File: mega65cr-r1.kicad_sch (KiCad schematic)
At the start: 0 parts

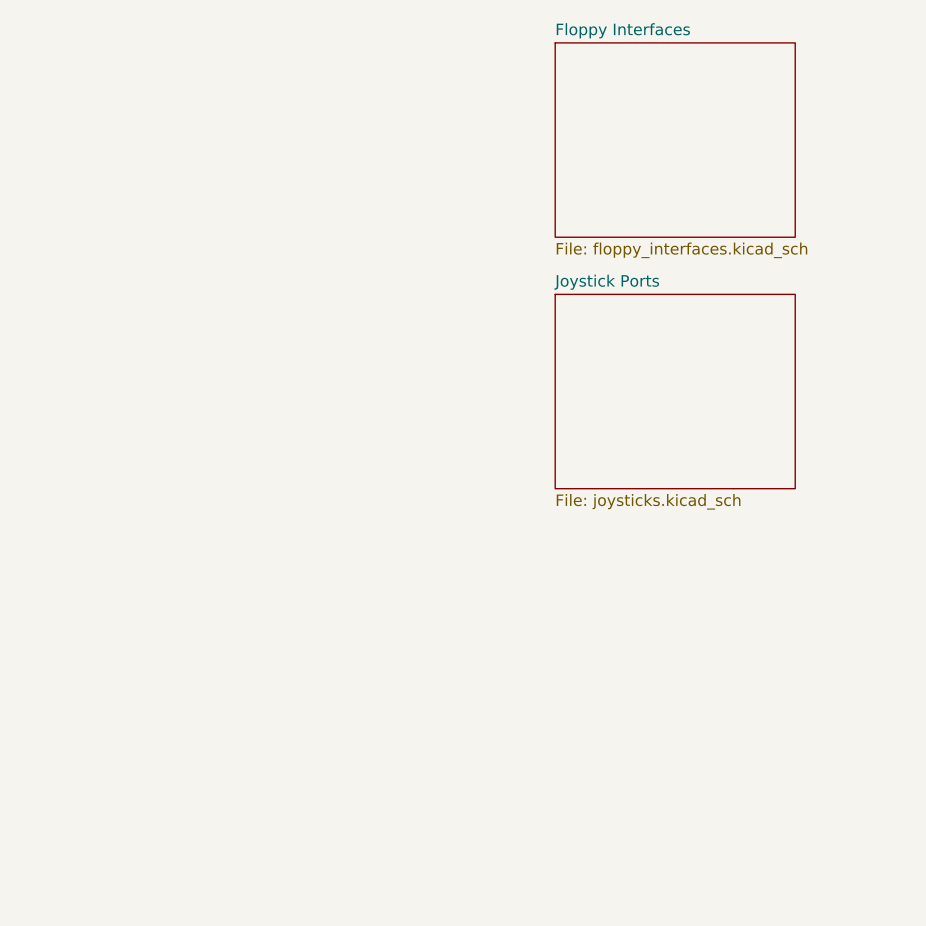
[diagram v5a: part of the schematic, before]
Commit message: add stubs for missing sheets
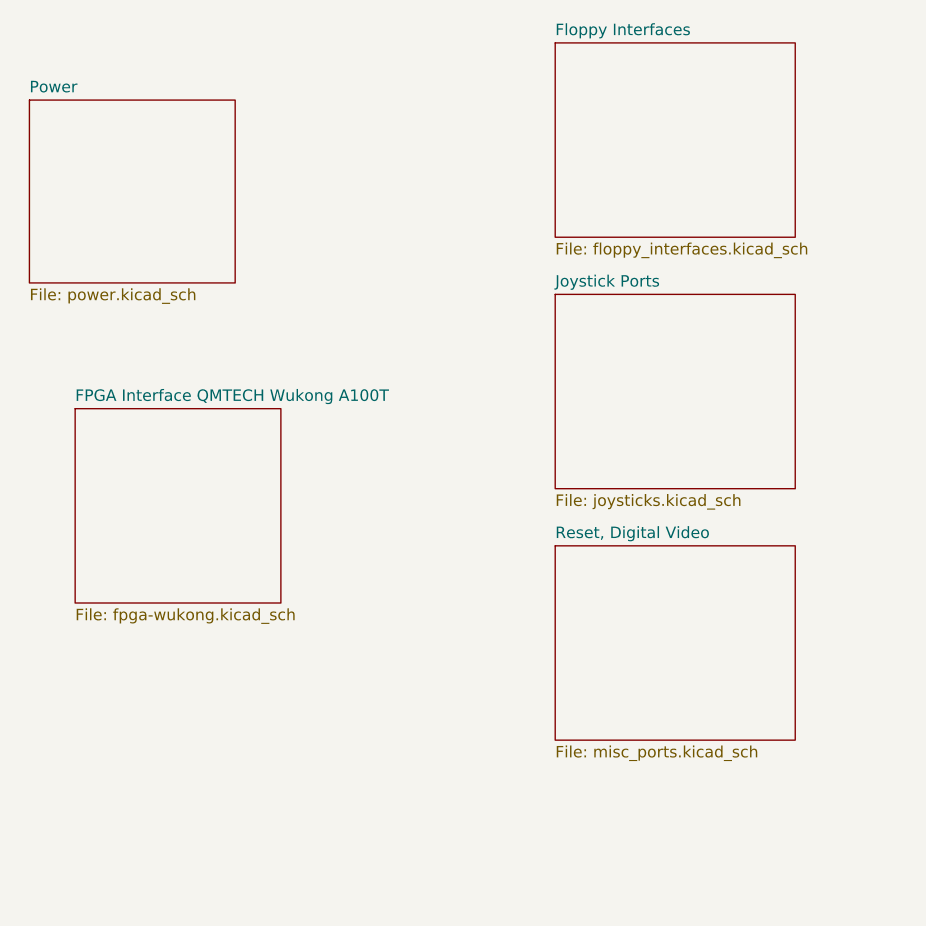
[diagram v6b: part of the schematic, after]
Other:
- added sheet FPGA Interface QMTECH Wukong A100T (fpga-wukong.kicad_sch)
- added sheet Power (power.kicad_sch)
- added sheet Reset, Digital Video (misc_ports.kicad_sch)
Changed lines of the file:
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@@
     (effects (font (size 1.27 1.27)) (justify left bottom))
+  )
+  (sheet (at 195.58 59.69) (size 22.86 21.59) (fields_autoplaced)
+    (stroke (width 0.1524) (type solid) (color 0 0 0 0))
+    (fill (color 0 0 0 0.0000))
+    (property "Sheet name" "FPGA Interface QMTECH Wukong A100T" (id 0) (at 195.58 58.9784 0)
+      (effects (font (size 1.27 1.27)) (justify left bottom))
+    )
+    (property "Sheet file" "fpga-wukong.kicad_sch" (id 1) (at 195.58 81.8646 0)
+      (effects (font (size 1.27 1.27)) (justify left top))
+    )
+  )
+  (sheet (at 248.92 74.93) (size 26.67 21.59) (fields_autoplaced)
+    (stroke (width 0.1524) (type solid) (color 0 0 0 0))
+    (fill (color 0 0 0 0.0000))
+    (property "Sheet name" "Reset, Digital Video" (id 0) (at 248.92 74.2184 0)
+      (effects (font (size 1.27 1.27)) (justify left bottom))
+    )
+    (property "Sheet file" "misc_ports.kicad_sch" (id 1) (at 248.92 97.1046 0)
+      (effects (font (size 1.27 1.27)) (justify left top))
+    )
   )
   (sheet (at 248.92 19.05) (size 26.67 21.59) (fields_autoplaced)
@@
     )
     (property "Sheet file" "floppy_interfaces.kicad_sch" (id 1) (at 248.92 41.2246 0)
+      (effects (font (size 1.27 1.27)) (justify left top))
+    )
+  )
+  (sheet (at 190.5 25.4) (size 22.86 20.32) (fields_autoplaced)
+    (stroke (width 0.1524) (type solid) (color 0 0 0 0))
+    (fill (color 0 0 0 0.0000))
+    (property "Sheet name" "Power" (id 0) (at 190.5 24.6884 0)
+      (effects (font (size 1.27 1.27)) (justify left bottom))
+    )
+    (property "Sheet file" "power.kicad_sch" (id 1) (at 190.5 46.3046 0)
       (effects (font (size 1.27 1.27)) (justify left top))
     )
@@
     (path "/bf6f0944-6234-4b84-bc75-6d48246ce101" (page "2"))
     (path "/ee5f4bc8-ae5c-44e7-a23d-2b06f471a294" (page "3"))
+    (path "/46f1890f-c5bb-4aae-8808-0511f47e29d8" (page "4"))
+    (path "/cd7afc30-e644-4a23-9f17-325d3146c7db" (page "5"))
+    (path "/2879178d-3b15-409b-b355-34424f0e3bd8" (page "6"))
   )
   (symbol_instances

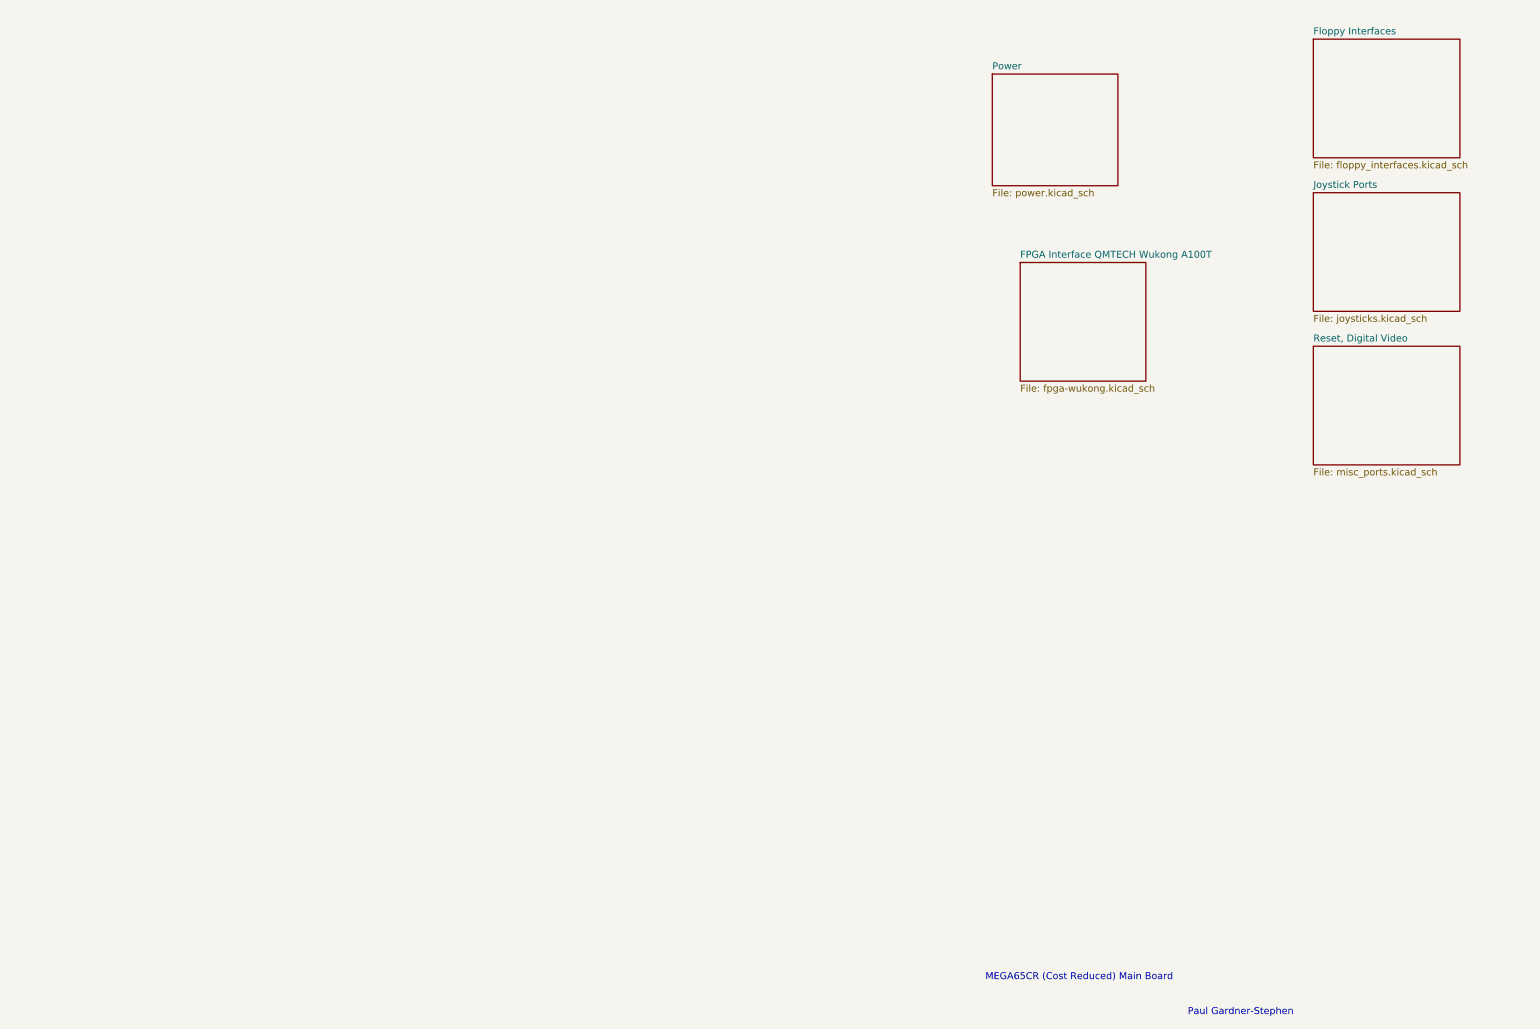
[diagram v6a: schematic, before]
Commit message: add sheets for expansion port, userport, VGA and multiplexor bus
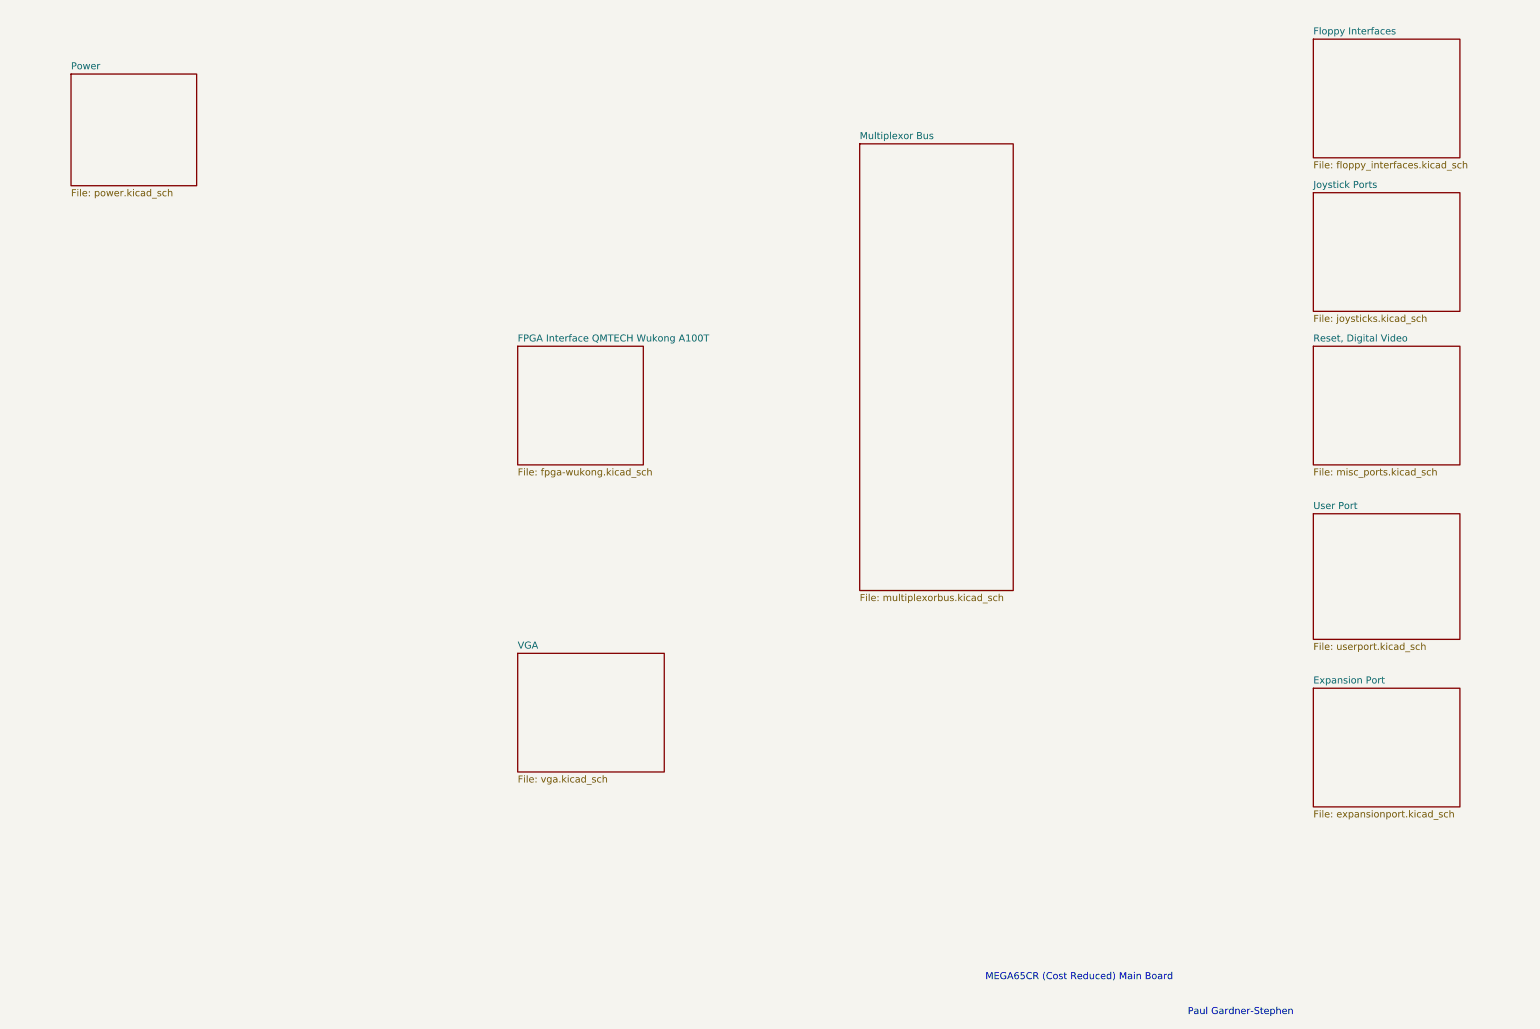
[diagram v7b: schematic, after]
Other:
- added sheet Expansion Port (expansionport.kicad_sch)
- added sheet Multiplexor Bus (multiplexorbus.kicad_sch)
- added sheet User Port (userport.kicad_sch)
- added sheet VGA (vga.kicad_sch)
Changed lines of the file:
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@@
     (effects (font (size 1.27 1.27)) (justify left bottom))
   )
-  (sheet (at 195.58 59.69) (size 22.86 21.59) (fields_autoplaced)
+  (sheet (at 248.92 105.41) (size 26.67 22.86) (fields_autoplaced)
     (stroke (width 0.1524) (type solid) (color 0 0 0 0))
     (fill (color 0 0 0 0.0000))
-    (property "Sheet name" "FPGA Interface QMTECH Wukong A100T" (id 0) (at 195.58 58.9784 0)
+    (property "Sheet name" "User Port" (id 0) (at 248.92 104.6984 0)
       (effects (font (size 1.27 1.27)) (justify left bottom))
     )
-    (property "Sheet file" "fpga-wukong.kicad_sch" (id 1) (at 195.58 81.8646 0)
+    (property "Sheet file" "userport.kicad_sch" (id 1) (at 248.92 128.8546 0)
+      (effects (font (size 1.27 1.27)) (justify left top))
+    )
+  )
+  (sheet (at 104.14 74.93) (size 22.86 21.59) (fields_autoplaced)
+    (stroke (width 0.1524) (type solid) (color 0 0 0 0))
+    (fill (color 0 0 0 0.0000))
+    (property "Sheet name" "FPGA Interface QMTECH Wukong A100T" (id 0) (at 104.14 74.2184 0)
+      (effects (font (size 1.27 1.27)) (justify left bottom))
+    )
+    (property "Sheet file" "fpga-wukong.kicad_sch" (id 1) (at 104.14 97.1046 0)
+      (effects (font (size 1.27 1.27)) (justify left top))
+    )
+  )
+  (sheet (at 104.14 130.81) (size 26.67 21.59) (fields_autoplaced)
+    (stroke (width 0.1524) (type solid) (color 0 0 0 0))
+    (fill (color 0 0 0 0.0000))
+    (property "Sheet name" "VGA" (id 0) (at 104.14 130.0984 0)
+      (effects (font (size 1.27 1.27)) (justify left bottom))
+    )
+    (property "Sheet file" "vga.kicad_sch" (id 1) (at 104.14 152.9846 0)
       (effects (font (size 1.27 1.27)) (justify left top))
     )
@@
     )
   )
+  (sheet (at 166.37 38.1) (size 27.94 81.28) (fields_autoplaced)
+    (stroke (width 0.1524) (type solid) (color 0 0 0 0))
+    (fill (color 0 0 0 0.0000))
+    (property "Sheet name" "Multiplexor Bus" (id 0) (at 166.37 37.3884 0)
+      (effects (font (size 1.27 1.27)) (justify left bottom))
+    )
+    (property "Sheet file" "multiplexorbus.kicad_sch" (id 1) (at 166.37 119.9646 0)
+      (effects (font (size 1.27 1.27)) (justify left top))
+    )
+  )
+  (sheet (at 248.92 137.16) (size 26.67 21.59) (fields_autoplaced)
+    (stroke (width 0.1524) (type solid) (color 0 0 0 0))
+    (fill (color 0 0 0 0.0000))
+    (property "Sheet name" "Expansion Port" (id 0) (at 248.92 136.4484 0)
+      (effects (font (size 1.27 1.27)) (justify left bottom))
+    )
+    (property "Sheet file" "expansionport.kicad_sch" (id 1) (at 248.92 159.3346 0)
+      (effects (font (size 1.27 1.27)) (justify left top))
+    )
+  )
   (sheet (at 248.92 19.05) (size 26.67 21.59) (fields_autoplaced)
     (stroke (width 0.1524) (type solid) (color 0 0 0 0))
@@
     )
   )
-  (sheet (at 190.5 25.4) (size 22.86 20.32) (fields_autoplaced)
+  (sheet (at 22.86 25.4) (size 22.86 20.32) (fields_autoplaced)
     (stroke (width 0.1524) (type solid) (color 0 0 0 0))
     (fill (color 0 0 0 0.0000))
-    (property "Sheet name" "Power" (id 0) (at 190.5 24.6884 0)
+    (property "Sheet name" "Power" (id 0) (at 22.86 24.6884 0)
       (effects (font (size 1.27 1.27)) (justify left bottom))
     )
-    (property "Sheet file" "power.kicad_sch" (id 1) (at 190.5 46.3046 0)
+    (property "Sheet file" "power.kicad_sch" (id 1) (at 22.86 46.3046 0)
       (effects (font (size 1.27 1.27)) (justify left top))
     )
@@
     (path "/cd7afc30-e644-4a23-9f17-325d3146c7db" (page "5"))
     (path "/2879178d-3b15-409b-b355-34424f0e3bd8" (page "6"))
+    (path "/021c7e3b-ea95-4afa-9d1d-76ae503bbd65" (page "7"))
+    (path "/48871385-9b55-4bb1-8319-1c951289d910" (page "8"))
+    (path "/601f3fca-6ee6-4b4f-870c-3e6d075cb571" (page "9"))
+    (path "/3e79ecec-be2d-46e5-9b86-3d84ade3f323" (page "10"))
   )
   (symbol_instances
